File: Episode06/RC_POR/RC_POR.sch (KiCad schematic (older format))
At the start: 4 parts, among them U1 74HC14

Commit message: minor improvements to schematic
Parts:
- C1: value 760 nF -> 1 uF
- D1: value D -> 1N4001
- R1: value 60K -> 50K
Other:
- note added: "Make sure this diode has\na reasonably small forward\nvoltage, and also that it can\npass enough current to\ndischarge the capacitor."
- note added: "The resistor and capacitor values are chosen with the goal\nthat the RC time constant is about 50 ms."
- note removed: "The resistor and capacitor values are chosen somewhat arbitrarily:\nthe goal is that the RC time constant is about 50 ms. (Using the\nvalues shown, the RC time constant will be about 45 ms.)"
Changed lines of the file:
@@
 EESchema Schematic File Version 4
+LIBS:RC_POR-cache
 EELAYER 26 0
 EELAYER END
@@
 P 3500 4150
 F 0 "C1" H 3615 4196 50  0000 L CNN
-F 1 "760 nF" H 3615 4105 50  0000 L CNN
+F 1 "1 uF" H 3615 4105 50  0000 L CNN
 F 2 "" H 3538 4000 50  0001 C CNN
 F 3 "" H 3500 4150 50  0001 C CNN
@@
 P 3500 3050
 F 0 "R1" H 3570 3096 50  0000 L CNN
-F 1 "60K" H 3570 3005 50  0000 L CNN
+F 1 "50K" H 3570 3005 50  0000 L CNN
 F 2 "" V 3430 3050 50  0001 C CNN
 F 3 "" H 3500 3050 50  0001 C CNN
@@
 P 2950 3050
 F 0 "D1" V 2904 3129 50  0000 L CNN
-F 1 "D" V 2995 3129 50  0000 L CNN
+F 1 "1N4001" V 2995 3129 50  0000 L CNN
 F 2 "" H 2950 3050 50  0001 C CNN
 F 3 "" H 2950 3050 50  0001 C CNN
@@
 RC power on reset circuit
 Text Notes 2400 5150 0    50   ~ 0
-The resistor and capacitor values are chosen somewhat arbitrarily:\nthe goal is that the RC time constant is about 50 ms.  (Using the\nvalues shown, the RC time constant will be about 45 ms.)
+The resistor and capacitor values are chosen with the goal\nthat the RC time constant is about 50 ms.
+Text Notes 1750 3200 0    50   ~ 0
+Make sure this diode has\na reasonably small forward\nvoltage, and also that it can\npass enough current to\ndischarge the capacitor.
 $EndSCHEMATC

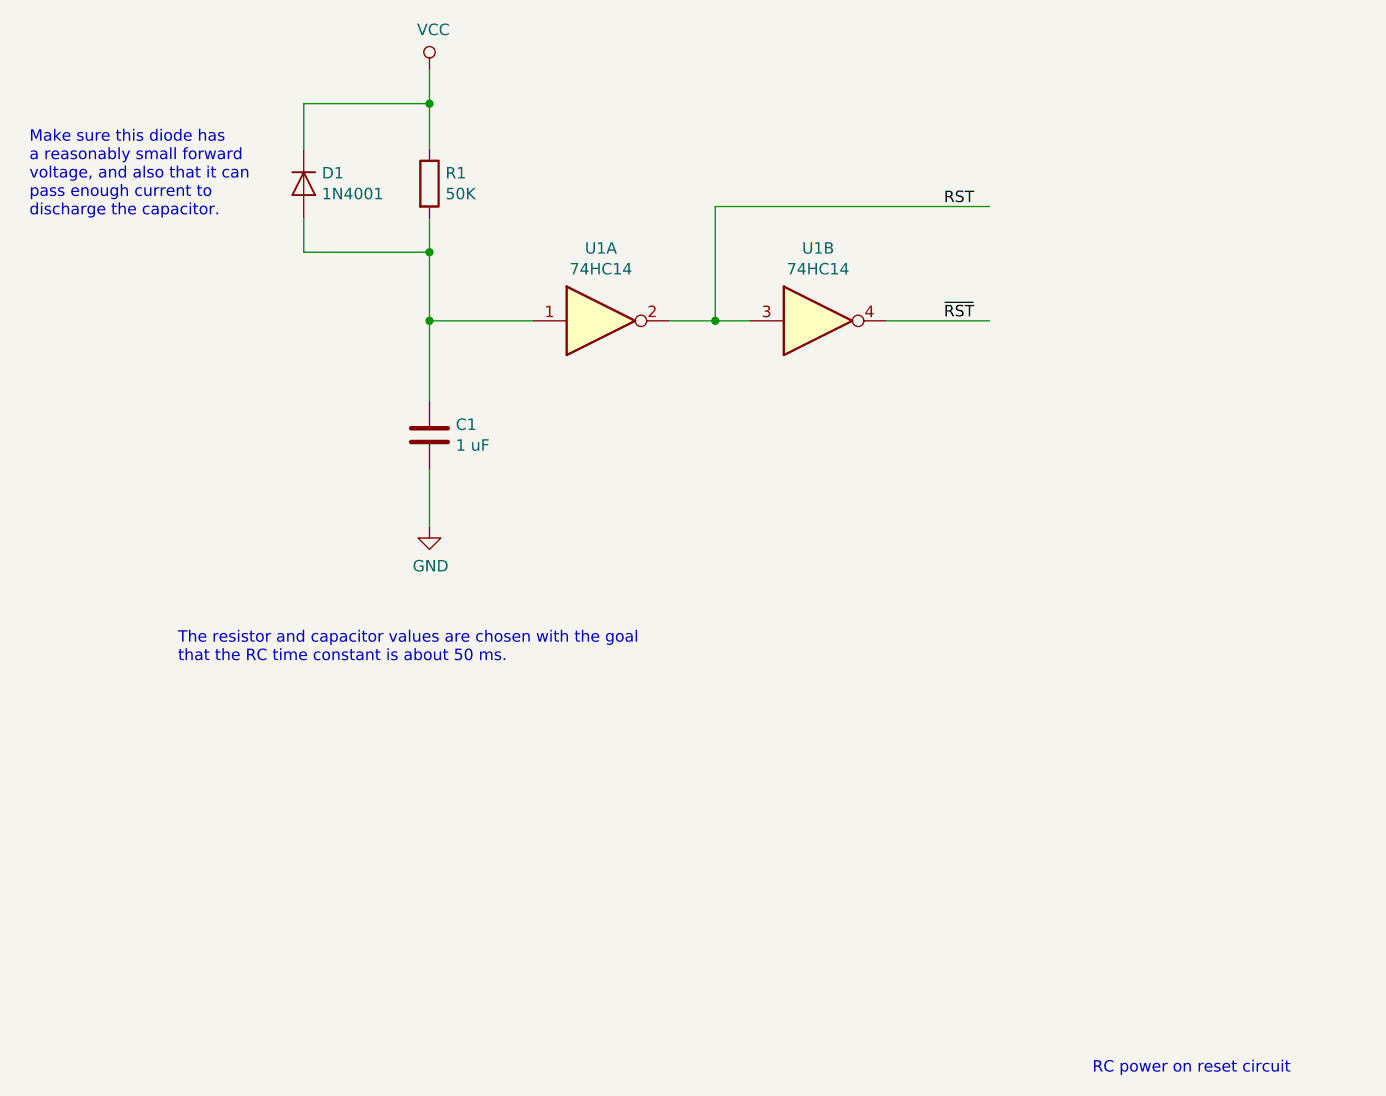
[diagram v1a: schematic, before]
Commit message: fix library path, use polarized cap
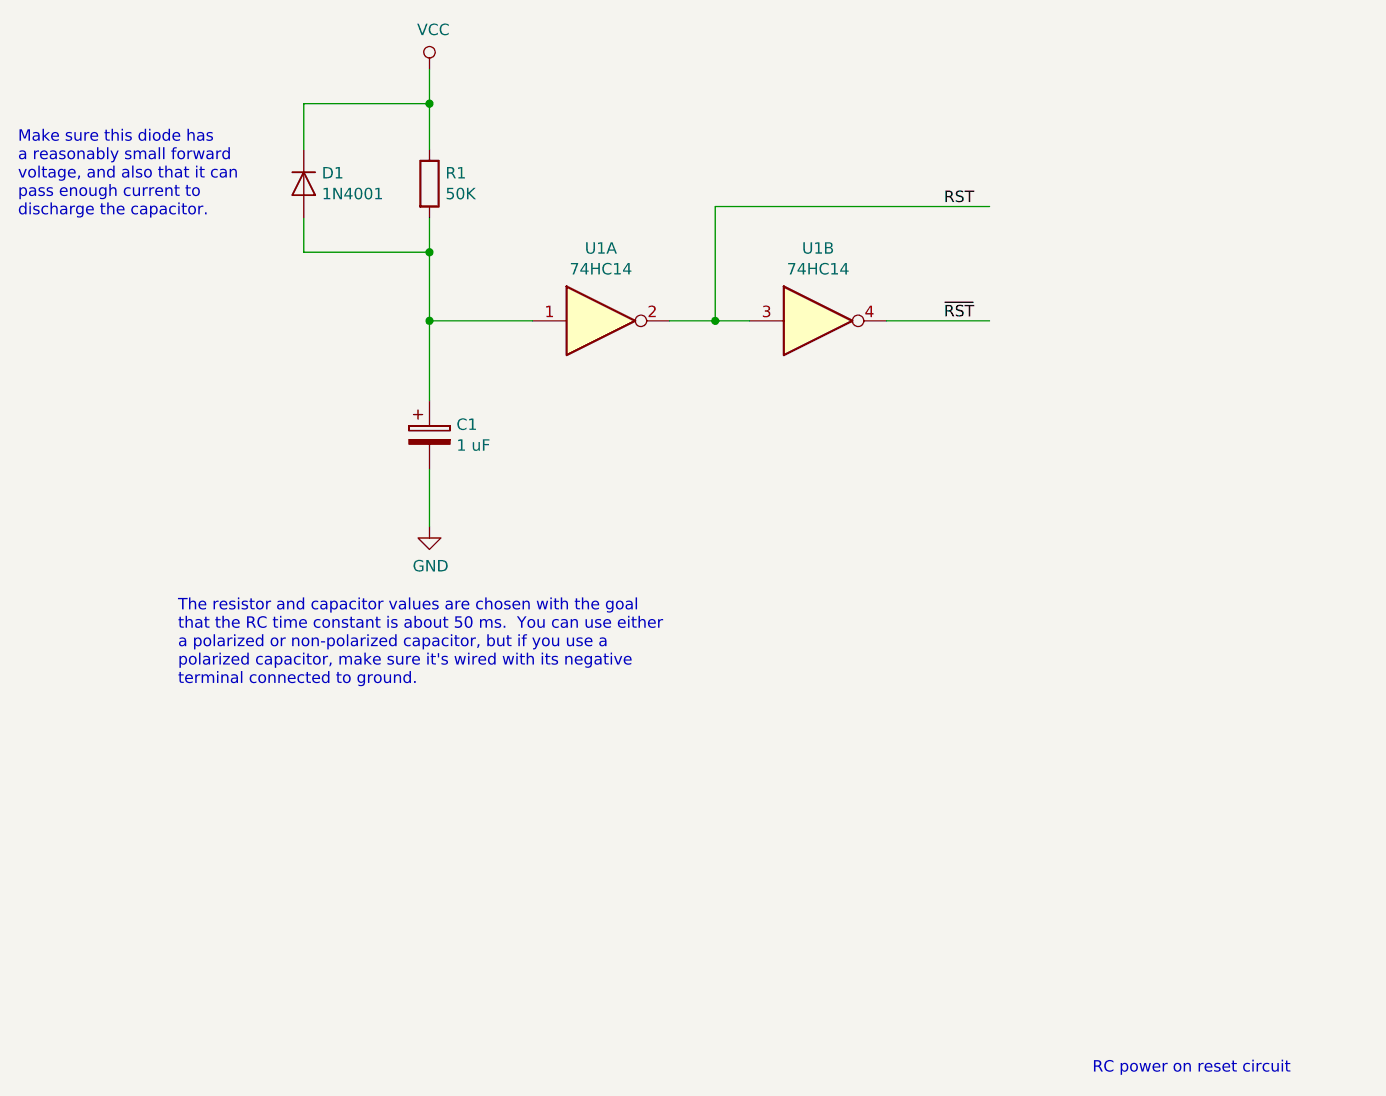
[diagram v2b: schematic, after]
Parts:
- removed C1: 1 uF, symbol device:C
- added C1: 1 uF, symbol device:CP
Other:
- note added: "The resistor and capacitor values are chosen with the goal\nthat the RC time constant is about 50 ms. You can use either\na polarized or non-polarized capacitor, but if you use a\npolarized capacitor, make sure it's wired with its negative\nterminal connected to ground."
- note removed: "The resistor and capacitor values are chosen with the goal\nthat the RC time constant is about 50 ms."
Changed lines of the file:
@@
 Comment4 ""
 $EndDescr
-$Comp
-L device:C C1
-U 1 1 5C683EF9
-P 3500 4150
-F 0 "C1" H 3615 4196 50  0000 L CNN
-F 1 "1 uF" H 3615 4105 50  0000 L CNN
-F 2 "" H 3538 4000 50  0001 C CNN
-F 3 "" H 3500 4150 50  0001 C CNN
-	1    3500 4150
-	1    0    0    -1
-$EndComp
 Wire Wire Line
 	3500 4300 3500 4550
@@
 Text Notes 6400 6950 0    50   ~ 0
 RC power on reset circuit
-Text Notes 2400 5150 0    50   ~ 0
-The resistor and capacitor values are chosen with the goal\nthat the RC time constant is about 50 ms.
-Text Notes 1750 3200 0    50   ~ 0
+Text Notes 2400 5250 0    50   ~ 0
+The resistor and capacitor values are chosen with the goal\nthat the RC time constant is about 50 ms.  You can use either\na polarized or non-polarized capacitor, but if you use a\npolarized capacitor, make sure it's wired with its negative\nterminal connected to ground.
+Text Notes 1700 3200 0    50   ~ 0
 Make sure this diode has\na reasonably small forward\nvoltage, and also that it can\npass enough current to\ndischarge the capacitor.
+$Comp
+L device:CP C1
+U 1 1 5C69625F
+P 3500 4150
+F 0 "C1" H 3618 4196 50  0000 L CNN
+F 1 "1 uF" H 3618 4105 50  0000 L CNN
+F 2 "" H 3538 4000 50  0001 C CNN
+F 3 "" H 3500 4150 50  0001 C CNN
+	1    3500 4150
+	1    0    0    -1
+$EndComp
 $EndSCHEMATC
